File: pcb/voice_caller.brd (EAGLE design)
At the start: 56.5 x 59.1 mm, 28 parts, among them IC1 PRO_MICRO, IC2 AT45DB321D-S, IC3 78L12SMD, K1 TQ2SA-L2-5V

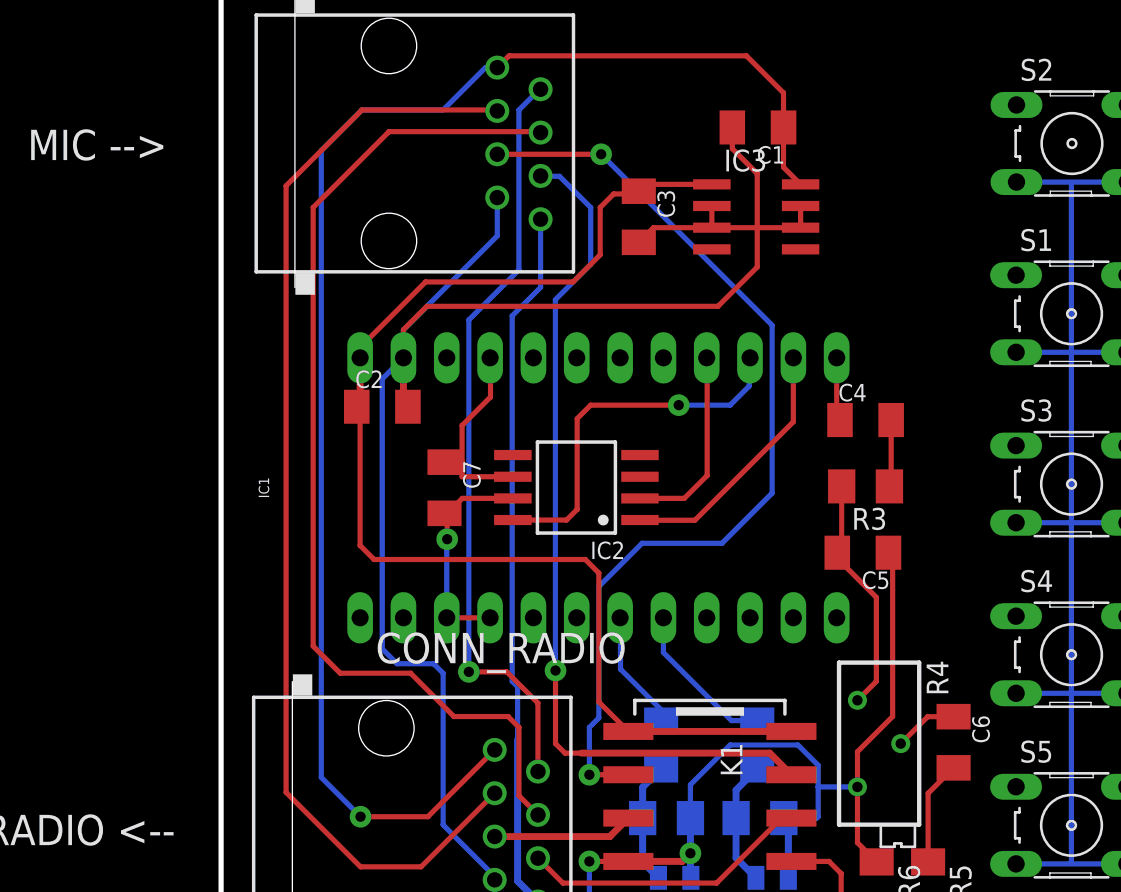
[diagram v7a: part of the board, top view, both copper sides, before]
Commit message: PTT circuit added
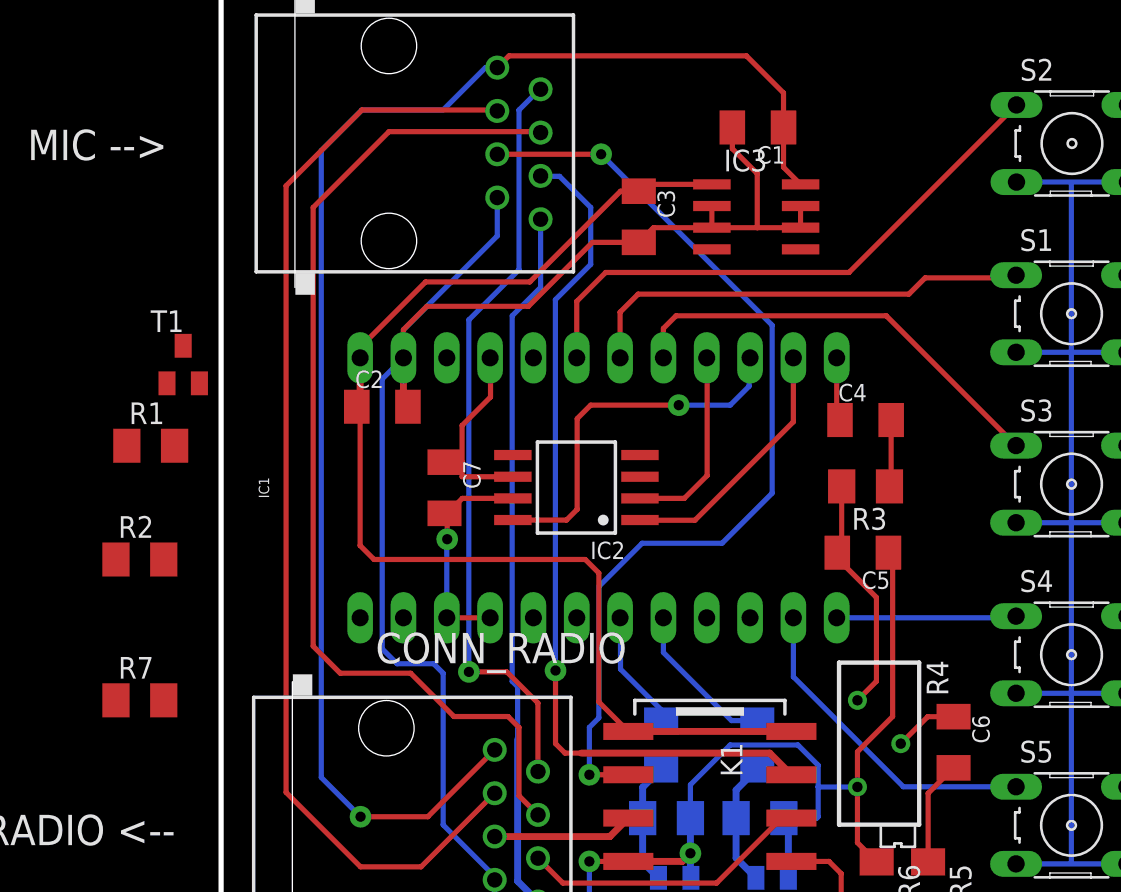
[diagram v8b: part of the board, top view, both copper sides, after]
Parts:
- added R1, R2, R7: (no value), rcl:M1206
- added T1: (no value), transistor:SOT23-BEC
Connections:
- removed net N$12: S4.1
- removed net N$15: S5.1
- removed net N$16: IC1.18
- removed net N$17: IC1.17
- removed net N$4: IC1.20
- removed net N$9: S3.1
- new net BUTTON3: IC1.17, S3.1
- new net BUTTON4: IC1.12, S4.1
- new net BUTTON5: IC1.11, S5.1
- new net PTT_SENSE: IC1.20, R1.2, T1.E
- new net PTT_SW: IC1.5, R2.2
- net BUTTON1: now also IC1.19
- net BUTTON2: now also IC1.18
- net GND: now also R1.1, R7.2
- net N$5: now also R2.1, R7.1, T1.B; no longer IC1.19
- net PTT: now also T1.C
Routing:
- net BUTTON1: track 0.00 -> 33.9 mm
- net BUTTON2: track 0.00 -> 26.8 mm
- net BUTTON3: track 0.00 -> 25.9 mm
- net BUTTON5: track 0.00 -> 19.2 mm
- net BUTTON4: track 0.00 -> 10.6 mm
- net GND: track 243.7 -> 235.2 mm
- net +5V: track 72.2 -> 70.8 mm
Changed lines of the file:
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@@
 <attribute name="OC_FARNELL" value="176432" x="56.205965625" y="15.21314375" size="1.778" layer="27" display="off"/>
 </element>
+<element name="T1" library="transistor" package="SOT23-BEC" value="" x="4.1275" y="42.2275"/>
+<element name="R1" library="rcl" package="M1206" value="" x="2.2225" y="37.465"/>
+<element name="R2" library="rcl" package="M1206" value="" x="1.5875" y="30.7975"/>
+<element name="R7" library="rcl" package="M1206" value="" x="1.5875" y="22.5425"/>
 </elements>
 <signals>
@@
 <wire x1="14.5" y1="42.62" x2="14.5" y2="43.23375" width="0.3048" layer="1"/>
 <wire x1="14.5" y1="43.23375" x2="18.335625" y2="47.069375" width="0.3048" layer="1"/>
-<wire x1="18.335625" y1="47.069375" x2="26.9875" y2="47.069375" width="0.3048" layer="1"/>
-<wire x1="26.9875" y1="47.069375" x2="28.575" y2="48.656875" width="0.3048" layer="1"/>
-<wire x1="28.575" y1="48.656875" x2="28.575" y2="51.435" width="0.3048" layer="1"/>
-<wire x1="28.575" y1="51.435" x2="29.36875" y2="52.22875" width="0.3048" layer="1"/>
-<wire x1="29.36875" y1="52.22875" x2="30.6775" y2="52.22875" width="0.3048" layer="1"/>
+<wire x1="18.335625" y1="47.069375" x2="24.4475" y2="47.069375" width="0.3048" layer="1"/>
+<wire x1="24.4475" y1="47.069375" x2="29.766875" y2="52.38875" width="0.3048" layer="1"/>
 <wire x1="30.6775" y1="52.22875" x2="30.8375" y2="52.38875" width="0.3048" layer="1"/>
 <wire x1="14.303696875" y1="39.752528125" x2="14.5" y2="39.752528125" width="0.4064" layer="1"/>
@@
 <wire x1="28.495625" y1="30.00375" x2="28.495625" y2="22.445625" width="0.3048" layer="1"/>
 <wire x1="28.495625" y1="22.445625" x2="30.224375" y2="20.716875" width="0.3048" layer="1"/>
+<wire x1="29.766875" y1="52.38875" x2="30.8375" y2="52.38875" width="0.3048" layer="1"/>
 </signal>
 <signal name="GND">
@@
 <wire x1="37.7825" y1="53.419375" x2="37.7825" y2="50.25" width="0.3048" layer="1"/>
 <wire x1="17.04" y1="44.265625" x2="18.415" y2="45.640625" width="0.3048" layer="1"/>
-<wire x1="18.415" y1="45.640625" x2="35.480625" y2="45.640625" width="0.3048" layer="1"/>
-<wire x1="35.480625" y1="45.640625" x2="37.7825" y2="47.9425" width="0.3048" layer="1"/>
-<wire x1="37.7825" y1="47.9425" x2="37.7825" y2="50.25" width="0.3048" layer="1"/>
+<wire x1="18.415" y1="45.640625" x2="24.368125" y2="45.640625" width="0.3048" layer="1"/>
+<wire x1="24.368125" y1="45.640625" x2="28.11625" y2="49.38875" width="0.3048" layer="1"/>
 <wire x1="22.12" y1="27.013125" x2="22.12" y2="27.38" width="0.3048" layer="1"/>
 <wire x1="17.04" y1="44.265625" x2="17.04" y2="42.62" width="0.3048" layer="1"/>
@@
 <wire x1="52.954765625" y1="12.95254375" x2="59.457165625" y2="12.95254375" width="0.3048" layer="16"/>
 <wire x1="56.1975" y1="52.705" x2="56.1975" y2="13.0175" width="0.3048" layer="16"/>
+<wire x1="30.8375" y1="49.2525" x2="30.8375" y2="49.38875" width="0.4064" layer="1"/>
+<wire x1="28.11625" y1="49.38875" x2="30.8375" y2="49.38875" width="0.3048" layer="1"/>
+<contactref element="R1" pad="1"/>
+<contactref element="R7" pad="2"/>
 <wire x1="56.1975" y1="52.705" x2="52.9813" y2="52.925025" width="0" layer="19" extent="16-16"/>
 <wire x1="52.954765625" y1="12.95254375" x2="56.1975" y2="13.0175" width="0" layer="19" extent="16-16"/>
@@
 <wire x1="52.957234375" y1="32.953740625" x2="45.72" y2="30.805625" width="0" layer="19" extent="1-1"/>
 <wire x1="59.45995" y1="42.943775" x2="59.4837" y2="52.925025" width="0" layer="19" extent="1-1"/>
+<wire x1="0.8225" y1="37.465" x2="22.38375" y2="9.763125" width="0" layer="19" extent="1-16"/>
+<wire x1="2.9875" y1="22.5425" x2="0.8225" y2="37.465" width="0" layer="19" extent="1-1"/>
 </signal>
 <signal name="MOSI">
@@
 <wire x1="23.8125" y1="20.955" x2="23.8125" y2="16.9425" width="0.3048" layer="1"/>
 <wire x1="23.8125" y1="16.9425" x2="24.93" y2="15.825" width="0.3048" layer="1"/>
+<contactref element="T1" pad="C"/>
+<wire x1="4.1275" y1="43.3275" x2="13.335" y2="24.13" width="0" layer="19" extent="1-1"/>
 </signal>
 <signal name="+8V">
@@
 <signal name="BUTTON2">
 <contactref element="S1" pad="1"/>
+<contactref element="IC1" pad="18"/>
+<wire x1="29.74" y1="42.62" x2="29.74" y2="45.2975" width="0.3048" layer="1"/>
+<wire x1="29.74" y1="45.2975" x2="30.7975" y2="46.355" width="0.3048" layer="1"/>
+<wire x1="30.7975" y1="46.355" x2="46.6725" y2="46.355" width="0.3048" layer="1"/>
+<wire x1="46.6725" y1="46.355" x2="47.625" y2="47.3075" width="0.3048" layer="1"/>
+<wire x1="47.625" y1="47.3075" x2="52.800075" y2="47.3075" width="0.3048" layer="1"/>
+<wire x1="52.800075" y1="47.3075" x2="52.95755" y2="47.464975" width="0.3048" layer="1"/>
 </signal>
 <signal name="BUTTON1">
 <contactref element="S2" pad="1"/>
-</signal>
-<signal name="N$9">
+<contactref element="IC1" pad="19"/>
+<wire x1="27.2" y1="42.62" x2="27.2" y2="45.9325" width="0.3048" layer="1"/>
+<wire x1="27.2" y1="45.9325" x2="28.8925" y2="47.625" width="0.3048" layer="1"/>
+<wire x1="28.8925" y1="47.625" x2="43.160075" y2="47.625" width="0.3048" layer="1"/>
+<wire x1="43.160075" y1="47.625" x2="52.9813" y2="57.446225" width="0.3048" layer="1"/>
+</signal>
+<signal name="PTT_SENSE">
+<contactref element="IC1" pad="20"/>
+<contactref element="T1" pad="E"/>
+<contactref element="R1" pad="2"/>
+<wire x1="5.0775" y1="41.1275" x2="24.66" y2="42.62" width="0" layer="19" extent="1-1"/>
+<wire x1="3.6225" y1="37.465" x2="5.0775" y2="41.1275" width="0" layer="19" extent="1-1"/>
+</signal>
+<signal name="BUTTON3">
+<contactref element="IC1" pad="17"/>
 <contactref element="S3" pad="1"/>
-</signal>
-<signal name="N$12">
+<wire x1="32.28" y1="42.62" x2="32.28" y2="44.345" width="0.3048" layer="1"/>
+<wire x1="32.28" y1="44.345" x2="33.02" y2="45.085" width="0.3048" layer="1"/>
+<wire x1="33.02" y1="45.085" x2="45.347175" y2="45.085" width="0.3048" layer="1"/>
+<wire x1="45.347175" y1="45.085" x2="52.957234375" y2="37.474940625" width="0.3048" layer="1"/>
+</signal>
+<signal name="BUTTON5">
+<contactref element="IC1" pad="11"/>
+<contactref element="S5" pad="1"/>
+<wire x1="52.954765625" y1="17.47374375" x2="46.34375625" y2="17.47374375" width="0.3048" layer="16"/>
+<wire x1="46.34375625" y1="17.47374375" x2="39.9" y2="23.9175" width="0.3048" layer="16"/>
+<wire x1="39.9" y1="23.9175" x2="39.9" y2="27.38" width="0.3048" layer="16"/>
+</signal>
+<signal name="BUTTON4">
+<contactref element="IC1" pad="12"/>
 <contactref element="S4" pad="1"/>
-</signal>
-<signal name="N$15">
-<contactref element="S5" pad="1"/>
-</signal>
-<signal name="N$4">
-<contactref element="IC1" pad="20"/>
+<wire x1="42.44" y1="27.38" x2="52.86229375" y2="27.38" width="0.3048" layer="16"/>
+<wire x1="52.86229375" y1="27.38" x2="52.957234375" y2="27.474940625" width="0.3048" layer="16"/>
+</signal>
+<signal name="PTT_SW">
+<contactref element="IC1" pad="5"/>
+<contactref element="R2" pad="2"/>
+<wire x1="2.9875" y1="30.7975" x2="24.66" y2="27.38" width="0" layer="19" extent="1-1"/>
 </signal>
 <signal name="N$5">
-<contactref element="IC1" pad="19"/>
-</signal>
-<signal name="N$16">
-<contactref element="IC1" pad="18"/>
-</signal>
-<signal name="N$17">
-<contactref element="IC1" pad="17"/>
+<contactref element="T1" pad="B"/>
+<contactref element="R2" pad="1"/>
+<contactref element="R7" pad="1"/>
+<wire x1="0.1875" y1="30.7975" x2="0.1875" y2="22.5425" width="0" layer="19" extent="1-1"/>
+<wire x1="3.1775" y1="41.1275" x2="0.1875" y2="30.7975" width="0" layer="19" extent="1-1"/>
 </signal>
 </signals>
